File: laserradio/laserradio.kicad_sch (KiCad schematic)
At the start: 89 parts, among them J1 USB4105-GF-A, J2 Conn_01x01_Female, J3 DEBUG, J4 RIGHT, SW1 SW_SPDT, SW2 SW_SPDT, U1 W25Q128JV, U2 RP2040, U3 MCP1702T-3302E_CB, U4 ADA4891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

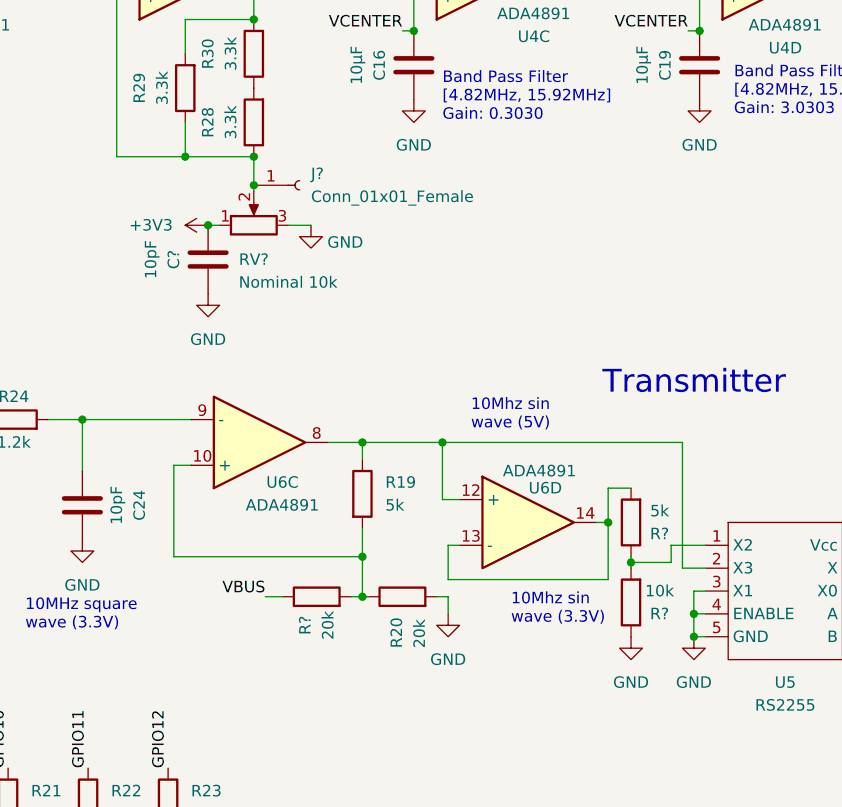
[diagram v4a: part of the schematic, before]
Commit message: update schematic
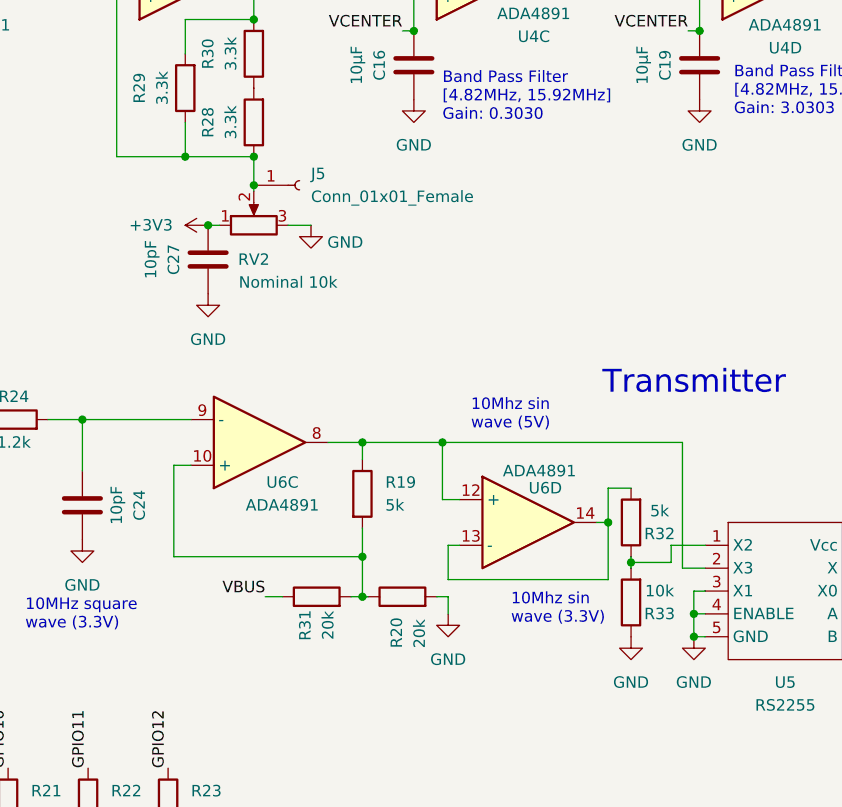
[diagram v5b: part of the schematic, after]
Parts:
- R31, R32, R33: renamed from R?; footprint (none) -> Resistor_SMD:R_0603_1608Metric
- gave numbers to parts that had none: 3
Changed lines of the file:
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@@
   (symbol (lib_id "Device:C") (at 206.375 105.41 0) (unit 1)
     (in_bom yes) (on_board yes)
-    (property "Reference" "C?" (id 0) (at 202.565 105.41 90))
+    (property "Reference" "C27" (id 0) (at 202.565 105.41 90))
     (property "Value" "10pF" (id 1) (at 200.025 105.41 90))
     (property "Footprint" "Capacitor_SMD:C_0603_1608Metric" (id 2) (at 207.3402 109.22 0)
@@
   (symbol (lib_id "Connector:Conn_01x01_Female") (at 216.535 97.155 0) (unit 1)
     (in_bom yes) (on_board yes) (fields_autoplaced)
-    (property "Reference" "J?" (id 0) (at 217.805 95.8849 0)
+    (property "Reference" "J5" (id 0) (at 217.805 95.8849 0)
       (effects (font (size 1.27 1.27)) (justify left))
     )
@@
   (symbol (lib_id "power:GND") (at 206.375 109.22 0) (unit 1)
     (in_bom yes) (on_board yes) (fields_autoplaced)
-    (property "Reference" "#PWR?" (id 0) (at 206.375 115.57 0)
+    (property "Reference" "#PWR056" (id 0) (at 206.375 115.57 0)
       (effects (font (size 1.27 1.27)) hide)
     )
@@
   (symbol (lib_id "Device:R") (at 253.365 134.62 180) (unit 1)
     (in_bom yes) (on_board yes)
-    (property "Reference" "R?" (id 0) (at 256.54 135.89 0))
+    (property "Reference" "R32" (id 0) (at 256.54 135.89 0))
     (property "Value" "5k" (id 1) (at 256.54 133.35 0))
-    (property "Footprint" "" (id 2) (at 255.143 134.62 90)
+    (property "Footprint" "Resistor_SMD:R_0603_1608Metric" (id 2) (at 255.143 134.62 90)
       (effects (font (size 1.27 1.27)) hide)
     )
@@
   (symbol (lib_id "power:+3V3") (at 206.375 101.6 90) (unit 1)
     (in_bom yes) (on_board yes)
-    (property "Reference" "#PWR?" (id 0) (at 210.185 101.6 0)
+    (property "Reference" "#PWR055" (id 0) (at 210.185 101.6 0)
       (effects (font (size 1.27 1.27)) hide)
     )
@@
   (symbol (lib_id "Device:R") (at 253.365 143.51 180) (unit 1)
     (in_bom yes) (on_board yes)
-    (property "Reference" "R?" (id 0) (at 256.54 144.78 0))
+    (property "Reference" "R33" (id 0) (at 256.54 144.78 0))
     (property "Value" "10k" (id 1) (at 256.54 142.24 0))
-    (property "Footprint" "" (id 2) (at 255.143 143.51 90)
+    (property "Footprint" "Resistor_SMD:R_0603_1608Metric" (id 2) (at 255.143 143.51 90)
       (effects (font (size 1.27 1.27)) hide)
     )
@@
   (symbol (lib_id "power:GND") (at 192.405 136.525 0) (unit 1)
     (in_bom yes) (on_board yes) (fields_autoplaced)
-    (property "Reference" "#PWR?" (id 0) (at 192.405 142.875 0)
+    (property "Reference" "#PWR050" (id 0) (at 192.405 142.875 0)
       (effects (font (size 1.27 1.27)) hide)
     )
@@
   (symbol (lib_id "power:GND") (at 217.805 101.6 0) (unit 1)
     (in_bom yes) (on_board yes)
-    (property "Reference" "#PWR?" (id 0) (at 217.805 107.95 0)
+    (property "Reference" "#PWR057" (id 0) (at 217.805 107.95 0)
       (effects (font (size 1.27 1.27)) hide)
     )
@@
   (symbol (lib_id "Device:R") (at 218.44 142.875 90) (unit 1)
     (in_bom yes) (on_board yes)
-    (property "Reference" "R?" (id 0) (at 217.17 146.05 0))
+    (property "Reference" "R31" (id 0) (at 217.17 146.05 0))
     (property "Value" "20k" (id 1) (at 219.71 146.05 0))
-    (property "Footprint" "" (id 2) (at 218.44 144.653 90)
+    (property "Footprint" "Resistor_SMD:R_0603_1608Metric" (id 2) (at 218.44 144.653 90)
       (effects (font (size 1.27 1.27)) hide)
     )
@@
   (symbol (lib_id "power:GND") (at 253.365 147.32 0) (unit 1)
     (in_bom yes) (on_board yes) (fields_autoplaced)
-    (property "Reference" "#PWR?" (id 0) (at 253.365 153.67 0)
+    (property "Reference" "#PWR058" (id 0) (at 253.365 153.67 0)
       (effects (font (size 1.27 1.27)) hide)
     )
@@
   (symbol (lib_id "Device:R_Potentiometer") (at 211.455 101.6 90) (unit 1)
     (in_bom yes) (on_board yes)
-    (property "Reference" "RV?" (id 0) (at 211.455 105.41 90))
+    (property "Reference" "RV2" (id 0) (at 211.455 105.41 90))
     (property "Value" "Nominal 10k" (id 1) (at 215.265 107.95 90))
     (property "Footprint" "Eclectronics:Laser Potentiometer" (id 2) (at 211.455 101.6 0)
@@
       (reference "#PWR049") (unit 1) (value "GND") (footprint "")
     )
+    (path "/9fe71ac4-1656-408f-b892-0e1738eab6c6"
+      (reference "#PWR050") (unit 1) (value "GND") (footprint "")
+    )
     (path "/45c78b5d-ae70-4c2e-aff3-ab840dd97db7"
       (reference "#PWR051") (unit 1) (value "GND") (footprint "")
@@
       (reference "#PWR054") (unit 1) (value "+3V3") (footprint "")
     )
+    (path "/7f1793be-08d2-4d6b-98b7-c56a8e5d54cc"
+      (reference "#PWR055") (unit 1) (value "+3V3") (footprint "")
+    )
+    (path "/6e76b6b7-3349-44c1-a4a6-89a43386c770"
+      (reference "#PWR056") (unit 1) (value "GND") (footprint "")
+    )
+    (path "/c1234ea3-4aa8-4457-815f-5441722e9a5a"
+      (reference "#PWR057") (unit 1) (value "GND") (footprint "")
+    )
+    (path "/f6bf6097-b262-4b5e-9513-19f21528a84d"
+      (reference "#PWR058") (unit 1) (value "GND") (footprint "")
+    )
     (path "/7ef8e1e6-062c-4651-bd2e-3b554bdfd161"
       (reference "#PWR0101") (unit 1) (value "+3V3") (footprint "")
@@
       (reference "#PWR0106") (unit 1) (value "GND") (footprint "")
     )
-    (path "/6e76b6b7-3349-44c1-a4a6-89a43386c770"
-      (reference "#PWR?") (unit 1) (value "GND") (footprint "")
-    )
-    (path "/7f1793be-08d2-4d6b-98b7-c56a8e5d54cc"
-      (reference "#PWR?") (unit 1) (value "+3V3") (footprint "")
-    )
-    (path "/9fe71ac4-1656-408f-b892-0e1738eab6c6"
-      (reference "#PWR?") (unit 1) (value "GND") (footprint "")
-    )
-    (path "/c1234ea3-4aa8-4457-815f-5441722e9a5a"
-      (reference "#PWR?") (unit 1) (value "GND") (footprint "")
-    )
-    (path "/f6bf6097-b262-4b5e-9513-19f21528a84d"
-      (reference "#PWR?") (unit 1) (value "GND") (footprint "")
-    )
     (path "/2fc9b624-be90-48f2-b80c-7987b933913b"
       (reference "C1") (unit 1) (value "0.1µF") (footprint "Capacitor_SMD:C_0603_1608Metric")
@@
     )
     (path "/2c9638f7-ec05-4d11-b2a2-982f4ff976da"
-      (reference "C?") (unit 1) (value "10pF") (footprint "Capacitor_SMD:C_0603_1608Metric")
+      (reference "C27") (unit 1) (value "10pF") (footprint "Capacitor_SMD:C_0603_1608Metric")
     )
     (path "/a4361543-0cee-4944-9d11-d5d7399a6613"
@@
     )
     (path "/5cbba035-48b3-4f41-a206-ec9418b43ddd"
-      (reference "J?") (unit 1) (value "Conn_01x01_Female") (footprint "Connector_PinHeader_2.54mm:PinHeader_1x01_P2.54mm_Vertical")
+      (reference "J5") (unit 1) (value "Conn_01x01_Female") (footprint "Connector_PinHeader_2.54mm:PinHeader_1x01_P2.54mm_Vertical")
     )
     (path "/eb3ee8cd-c148-4e58-8146-7d26f3c6b393"
@@
       (reference "R30") (unit 1) (value "3.3k") (footprint "Resistor_SMD:R_0603_1608Metric")
     )
+    (path "/c23fa5a2-6cc6-494c-b9a0-bdc86350a118"
+      (reference "R31") (unit 1) (value "20k") (footprint "Resistor_SMD:R_0603_1608Metric")
+    )
     (path "/7ed0f30a-56dd-4307-a4b3-3b90d15db2b1"
-      (reference "R?") (unit 1) (value "5k") (footprint "")
+      (reference "R32") (unit 1) (value "5k") (footprint "Resistor_SMD:R_0603_1608Metric")
     )
     (path "/953e8c6f-6f43-43b5-aad0-f05c0e1e28ff"
-      (reference "R?") (unit 1) (value "10k") (footprint "")
-    )
-    (path "/c23fa5a2-6cc6-494c-b9a0-bdc86350a118"
-      (reference "R?") (unit 1) (value "20k") (footprint "")
+      (reference "R33") (unit 1) (value "10k") (footprint "Resistor_SMD:R_0603_1608Metric")
     )
     (path "/3b2cc5a8-07b8-447e-bd99-41cd5649610a"
@@
     )
     (path "/f7a9ca89-59b8-4296-88a0-ee86b967a209"
-      (reference "RV?") (unit 1) (value "Nominal 10k") (footprint "Eclectronics:Laser Potentiometer")
+      (reference "RV2") (unit 1) (value "Nominal 10k") (footprint "Eclectronics:Laser Potentiometer")
     )
     (path "/2496860e-d9c9-4f6c-859d-6fa4659d70a0"

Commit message: Finalized schematic
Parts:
- added C?: 10pF, Capacitor_SMD:C_0603_1608Metric, symbol Device:C
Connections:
- net GND: now also C?.2
- net VBUS: now also C?.1
- net at C24.1, R24.2: now also U6.10 (+); no longer U6.9 (-)
- net at J5.1 (Pin_1), R28.1, R29.1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: now also U4.6 (-); no longer U4.5 (+)
- net at R19.2, R20.1, R31.2: now also U6.9 (-); no longer U6.10 (+)
- net at R26.2, R27.2, U4.1: now also U4.5 (+); no longer U4.6 (-)
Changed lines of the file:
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@@
     (company "Olin College of Engineering")
   )
+  (junction (at 213.995 142.875) (diameter 0) (color 0 0 0 0)
+  )
   (junction (at 67.31 130.81) (diameter 0) (color 0 0 0 0)
   )
@@
     (stroke (width 0) (type default) (color 0 0 0 0))
   )
-  (wire (pts (xy 214.63 142.875) (xy 212.725 142.875))
+  (wire (pts (xy 214.63 142.875) (xy 213.995 142.875))
     (stroke (width 0) (type default) (color 0 0 0 0))
   )
@@
     (stroke (width 0) (type default) (color 0 0 0 0))
   )
+  (wire (pts (xy 213.995 142.875) (xy 212.725 142.875))
+    (stroke (width 0) (type default) (color 0 0 0 0))
+  )
   (wire (pts (xy 240.665 64.77) (xy 244.475 64.77))
     (stroke (width 0) (type default) (color 0 0 0 0))
@@
     (pin "2")
   )
+  (symbol (lib_id "power:GND") (at 213.995 150.495 0) (unit 1)
+    (in_bom yes) (on_board yes) (fields_autoplaced)
+    (property "Reference" "#PWR?" (id 0) (at 213.995 156.845 0)
+      (effects (font (size 1.27 1.27)) hide)
+    )
+    (property "Value" "GND" (id 1) (at 213.995 155.575 0))
+    (property "Footprint" "" (id 2) (at 213.995 150.495 0)
+      (effects (font (size 1.27 1.27)) hide)
+    )
+    (property "Datasheet" "" (id 3) (at 213.995 150.495 0)
+      (effects (font (size 1.27 1.27)) hide)
+    )
+    (pin "1")
+  )
   (symbol (lib_id "Device:C") (at 74.93 140.97 270) (unit 1)
     (in_bom yes) (on_board yes)
@@
     (pin "1")
   )
-  (symbol (lib_id "Device:Opamp_Quad") (at 212.09 125.73 0) (mirror x) (unit 3)
+  (symbol (lib_id "Device:Opamp_Quad") (at 212.09 125.73 0) (unit 3)
     (in_bom yes) (on_board yes)
-    (property "Reference" "U6" (id 0) (at 214.63 130.175 0))
-    (property "Value" "ADA4891" (id 1) (at 214.63 132.715 0))
+    (property "Reference" "U6" (id 0) (at 214.63 133.35 0))
+    (property "Value" "ADA4891" (id 1) (at 214.63 130.81 0))
     (property "Footprint" "Package_SO:SOIC-14_3.9x8.7mm_P1.27mm" (id 2) (at 212.09 125.73 0)
       (effects (font (size 1.27 1.27)) hide)
@@
     (pin "1")
   )
-  (symbol (lib_id "Device:Opamp_Quad") (at 203.835 73.66 0) (mirror x) (unit 2)
+  (symbol (lib_id "Device:Opamp_Quad") (at 203.835 73.66 0) (unit 2)
     (in_bom yes) (on_board yes)
-    (property "Reference" "U4" (id 0) (at 204.47 65.405 0))
-    (property "Value" "ADA4891" (id 1) (at 205.74 67.945 0))
+    (property "Reference" "U4" (id 0) (at 206.375 69.215 0))
+    (property "Value" "ADA4891" (id 1) (at 206.375 66.675 0))
     (property "Footprint" "Package_SO:SOIC-14_3.9x8.7mm_P1.27mm" (id 2) (at 203.835 73.66 0)
       (effects (font (size 1.27 1.27)) hide)
@@
     (pin "2")
   )
+  (symbol (lib_id "Device:C") (at 213.995 146.685 0) (unit 1)
+    (in_bom yes) (on_board yes)
+    (property "Reference" "C?" (id 0) (at 210.185 146.685 90))
+    (property "Value" "10pF" (id 1) (at 207.645 146.685 90))
+    (property "Footprint" "Capacitor_SMD:C_0603_1608Metric" (id 2) (at 214.9602 150.495 0)
+      (effects (font (size 1.27 1.27)) hide)
+    )
+    (property "Datasheet" "~" (id 3) (at 213.995 146.685 0)
+      (effects (font (size 1.27 1.27)) hide)
+    )
+    (pin "1")
+    (pin "2")
+  )
   (symbol (lib_id "Eclectronics:RS2255") (at 270.51 142.24 0) (unit 1)
     (in_bom yes) (on_board yes)
@@
       (reference "#PWR0106") (unit 1) (value "GND") (footprint "")
     )
+    (path "/28373a2c-caa6-482c-a6ca-1c408f55d1be"
+      (reference "#PWR?") (unit 1) (value "GND") (footprint "")
+    )
     (path "/2fc9b624-be90-48f2-b80c-7987b933913b"
       (reference "C1") (unit 1) (value "0.1µF") (footprint "Capacitor_SMD:C_0603_1608Metric")
@@
       (reference "C27") (unit 1) (value "10pF") (footprint "Capacitor_SMD:C_0603_1608Metric")
     )
+    (path "/ed5b243e-e785-4808-9b98-c621d6a7eead"
+      (reference "C?") (unit 1) (value "10pF") (footprint "Capacitor_SMD:C_0603_1608Metric")
+    )
     (path "/a4361543-0cee-4944-9d11-d5d7399a6613"

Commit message: Mid work upload
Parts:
- gave numbers to parts that had none: 1
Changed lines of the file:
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@@
   (symbol (lib_id "power:GND") (at 213.995 150.495 0) (unit 1)
     (in_bom yes) (on_board yes) (fields_autoplaced)
-    (property "Reference" "#PWR?" (id 0) (at 213.995 156.845 0)
+    (property "Reference" "#PWR0107" (id 0) (at 213.995 156.845 0)
       (effects (font (size 1.27 1.27)) hide)
     )
@@
   (symbol (lib_id "Device:C") (at 213.995 146.685 0) (unit 1)
     (in_bom yes) (on_board yes)
-    (property "Reference" "C?" (id 0) (at 210.185 146.685 90))
+    (property "Reference" "C28" (id 0) (at 210.185 146.685 90))
     (property "Value" "10pF" (id 1) (at 207.645 146.685 90))
     (property "Footprint" "Capacitor_SMD:C_0603_1608Metric" (id 2) (at 214.9602 150.495 0)
@@
     )
     (path "/28373a2c-caa6-482c-a6ca-1c408f55d1be"
-      (reference "#PWR?") (unit 1) (value "GND") (footprint "")
+      (reference "#PWR0107") (unit 1) (value "GND") (footprint "")
     )
     (path "/2fc9b624-be90-48f2-b80c-7987b933913b"
@@
     )
     (path "/ed5b243e-e785-4808-9b98-c621d6a7eead"
-      (reference "C?") (unit 1) (value "10pF") (footprint "Capacitor_SMD:C_0603_1608Metric")
+      (reference "C28") (unit 1) (value "10pF") (footprint "Capacitor_SMD:C_0603_1608Metric")
     )
     (path "/a4361543-0cee-4944-9d11-d5d7399a6613"

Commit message: Major layout changes
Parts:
- removed C16: 10µF, Capacitor_SMD:C_0603_1608Metric, symbol Device:C
- renumbered J5 to Rx-Center1, J2 to Rx-Thresh1
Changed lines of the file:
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@@
     (stroke (width 0) (type default) (color 0 0 0 0))
   )
-  (wire (pts (xy 259.715 80.01) (xy 260.985 80.01))
+  (wire (pts (xy 229.235 80.01) (xy 260.985 80.01))
     (stroke (width 0) (type default) (color 0 0 0 0))
   )
@@
     (effects (font (size 1.27 1.27)) (justify right bottom))
   )
-  (label "VCENTER" (at 259.715 80.01 180)
-    (effects (font (size 1.27 1.27)) (justify right bottom))
-  )
   (label "GPIO10" (at 184.15 161.925 90)
     (effects (font (size 1.27 1.27)) (justify left bottom))
@@
   (symbol (lib_id "Connector:Conn_01x01_Female") (at 216.535 97.155 0) (unit 1)
     (in_bom yes) (on_board yes) (fields_autoplaced)
-    (property "Reference" "J5" (id 0) (at 217.805 95.8849 0)
+    (property "Reference" "Rx-Center1" (id 0) (at 218.44 95.8849 0)
       (effects (font (size 1.27 1.27)) (justify left))
     )
-    (property "Value" "Conn_01x01_Female" (id 1) (at 217.805 98.4249 0)
+    (property "Value" "Conn_01x01_Female" (id 1) (at 218.44 98.4249 0)
       (effects (font (size 1.27 1.27)) (justify left))
     )
@@
     (pin "1")
   )
-  (symbol (lib_id "power:GND") (at 229.235 87.63 0) (unit 1)
-    (in_bom yes) (on_board yes)
-    (property "Reference" "#PWR031" (id 0) (at 229.235 93.98 0)
-      (effects (font (size 1.27 1.27)) hide)
-    )
-    (property "Value" "GND" (id 1) (at 229.235 92.71 0))
-    (property "Footprint" "" (id 2) (at 229.235 87.63 0)
-      (effects (font (size 1.27 1.27)) hide)
-    )
-    (property "Datasheet" "" (id 3) (at 229.235 87.63 0)
-      (effects (font (size 1.27 1.27)) hide)
-    )
-    (pin "1")
-  )
   (symbol (lib_id "Device:LED_Filled") (at 184.15 173.355 90) (unit 1)
     (in_bom yes) (on_board yes) (fields_autoplaced)
@@
   (symbol (lib_id "Connector:Conn_01x01_Female") (at 322.58 81.915 0) (unit 1)
     (in_bom yes) (on_board yes) (fields_autoplaced)
-    (property "Reference" "J2" (id 0) (at 323.85 80.6449 0)
+    (property "Reference" "Rx-Thresh1" (id 0) (at 323.85 80.6449 0)
       (effects (font (size 1.27 1.27)) (justify left))
     )
@@
     (pin "2")
   )
-  (symbol (lib_id "Device:C") (at 229.235 83.82 0) (unit 1)
-    (in_bom yes) (on_board yes)
-    (property "Reference" "C16" (id 0) (at 225.425 83.82 90))
-    (property "Value" "10µF" (id 1) (at 222.885 83.82 90))
-    (property "Footprint" "Capacitor_SMD:C_0603_1608Metric" (id 2) (at 230.2002 87.63 0)
-      (effects (font (size 1.27 1.27)) hide)
-    )
-    (property "Datasheet" "~" (id 3) (at 229.235 83.82 0)
-      (effects (font (size 1.27 1.27)) hide)
-    )
-    (pin "1")
-    (pin "2")
-  )
   (symbol (lib_id "Device:LED_Filled") (at 193.04 173.355 90) (unit 1)
     (in_bom yes) (on_board yes) (fields_autoplaced)
@@
       (reference "#PWR030") (unit 1) (value "GND") (footprint "")
     )
-    (path "/8a003a61-ef55-45ba-ba36-6f6f9ae2e660"
-      (reference "#PWR031") (unit 1) (value "GND") (footprint "")
-    )
     (path "/daa07dde-5dfa-4b04-a33f-36d83dcf9b17"
       (reference "#PWR032") (unit 1) (value "GND") (footprint "")
@@
       (reference "C15") (unit 1) (value "10pF") (footprint "Capacitor_SMD:C_0603_1608Metric")
     )
-    (path "/e871d87f-a00a-4f3c-9ffc-b1d6b3b09630"
-      (reference "C16") (unit 1) (value "10µF") (footprint "Capacitor_SMD:C_0603_1608Metric")
-    )
     (path "/6a95f862-9a9f-4be7-8003-9949da1db22b"
       (reference "C17") (unit 1) (value "10pF") (footprint "Capacitor_SMD:C_0603_1608Metric")
@@
       (reference "J1") (unit 1) (value "USB4105-GF-A") (footprint "Eclectronics:USB4105-GF-A")
     )
-    (path "/8bbc4f14-1425-43e1-89e1-430bd22864f8"
-      (reference "J2") (unit 1) (value "Conn_01x01_Female") (footprint "Connector_PinHeader_2.54mm:PinHeader_1x01_P2.54mm_Vertical")
-    )
     (path "/071be64b-505f-4bfb-8d7b-0cbe248aadcc"
       (reference "J3") (unit 1) (value "DEBUG") (footprint "Connector_PinHeader_2.54mm:PinHeader_1x03_P2.54mm_Vertical")
@@
       (reference "J4") (unit 1) (value "RIGHT") (footprint "Connector_PinHeader_2.54mm:PinHeader_1x20_P2.54mm_Vertical")
     )
-    (path "/5cbba035-48b3-4f41-a206-ec9418b43ddd"
-      (reference "J5") (unit 1) (value "Conn_01x01_Female") (footprint "Connector_PinHeader_2.54mm:PinHeader_1x01_P2.54mm_Vertical")
-    )
     (path "/eb3ee8cd-c148-4e58-8146-7d26f3c6b393"
       (reference "LD1") (unit 1) (value "D_Laser_1A3C") (footprint "Connector_PinHeader_2.54mm:PinHeader_1x02_P2.54mm_Vertical")
@@
       (reference "RV2") (unit 1) (value "Nominal 10k") (footprint "Eclectronics:Laser Potentiometer")
     )
+    (path "/5cbba035-48b3-4f41-a206-ec9418b43ddd"
+      (reference "Rx-Center1") (unit 1) (value "Conn_01x01_Female") (footprint "Connector_PinHeader_2.54mm:PinHeader_1x01_P2.54mm_Vertical")
+    )
+    (path "/8bbc4f14-1425-43e1-89e1-430bd22864f8"
+      (reference "Rx-Thresh1") (unit 1) (value "Conn_01x01_Female") (footprint "Connector_PinHeader_2.54mm:PinHeader_1x01_P2.54mm_Vertical")
+    )
     (path "/2496860e-d9c9-4f6c-859d-6fa4659d70a0"
